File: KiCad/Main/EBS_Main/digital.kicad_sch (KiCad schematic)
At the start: 5 parts

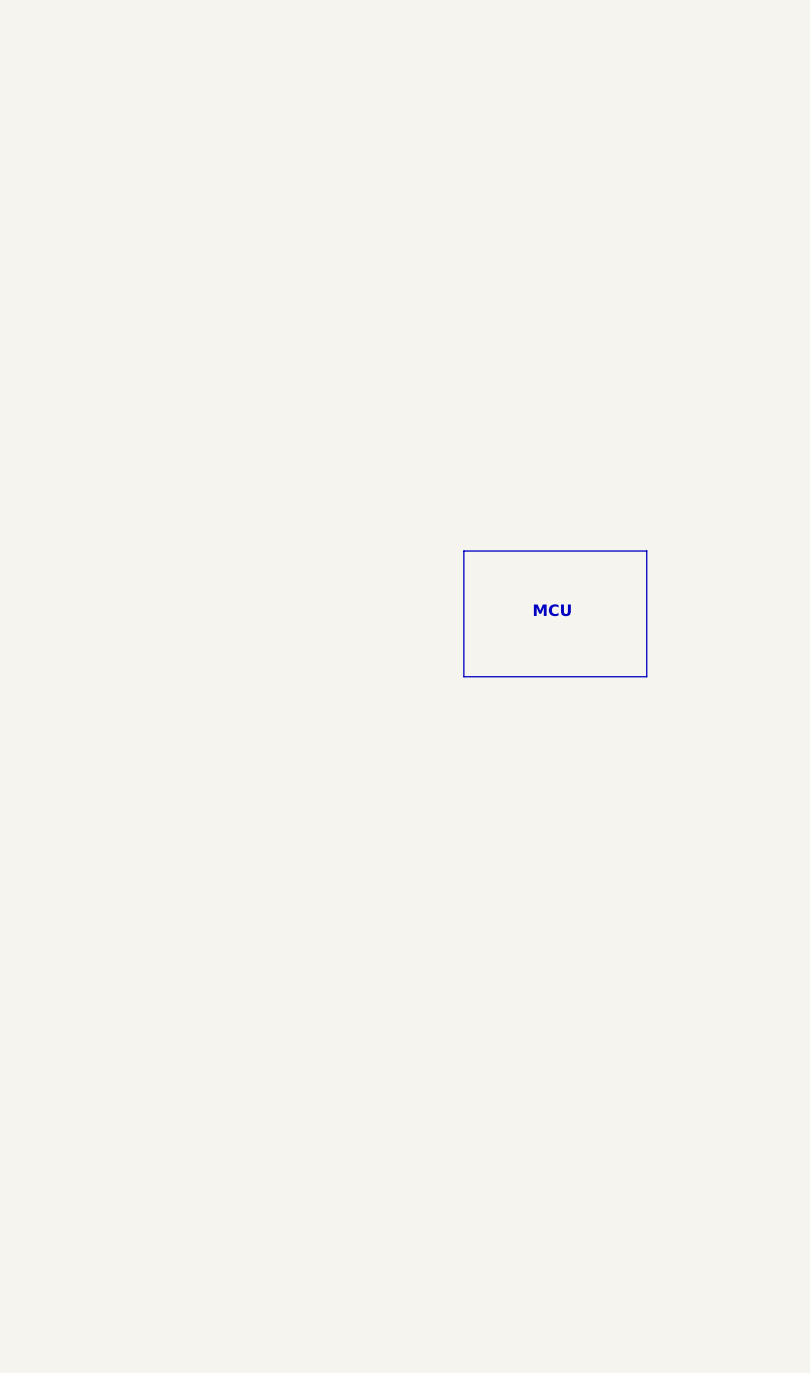
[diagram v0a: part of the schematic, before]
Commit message: found the fpga footprint and added it on schematic
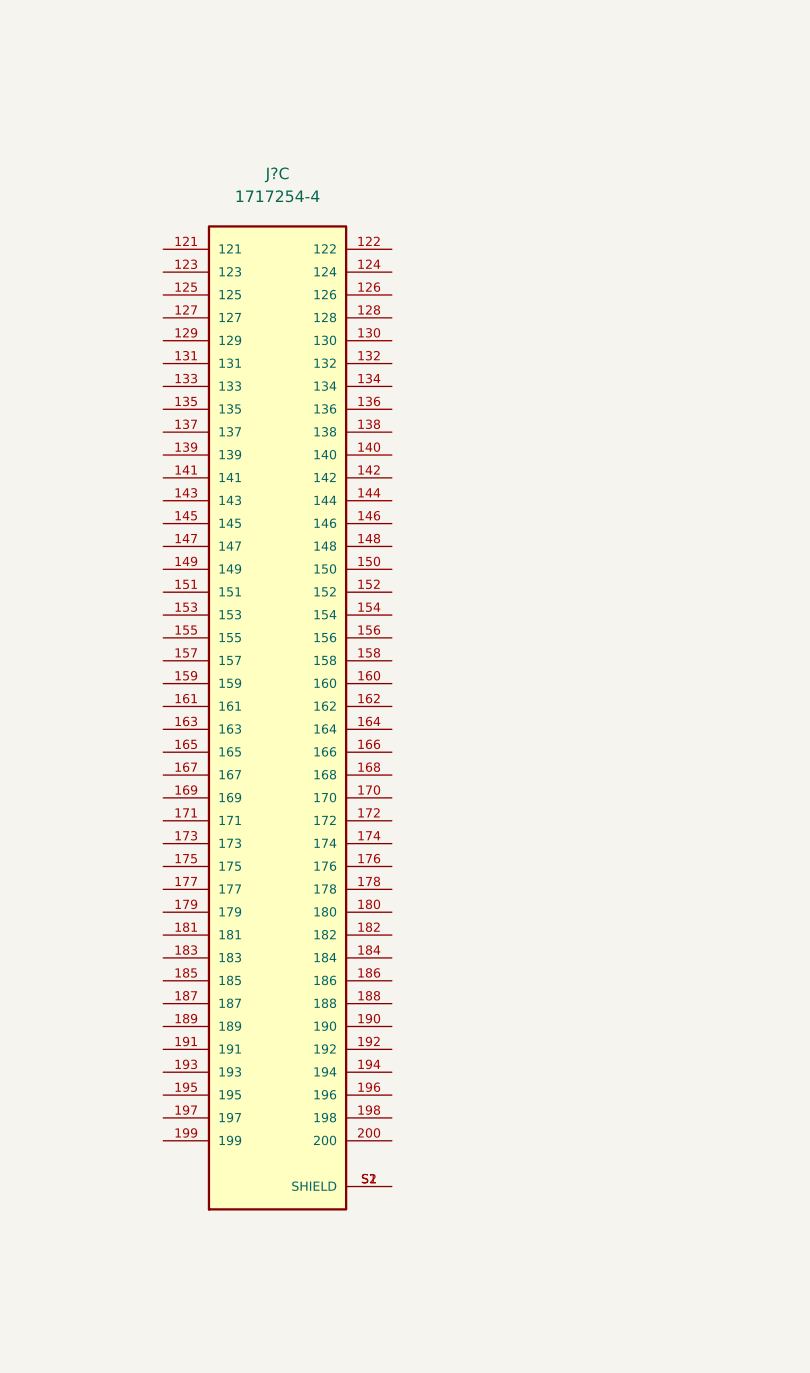
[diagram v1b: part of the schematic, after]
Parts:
- added J?: 1717254-4, TE_1717254-4, symbol 1717254-4:1717254-4
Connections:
- new net: J?.S1 (SHIELD), J?.S2 (SHIELD)
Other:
- note removed: "MCU"

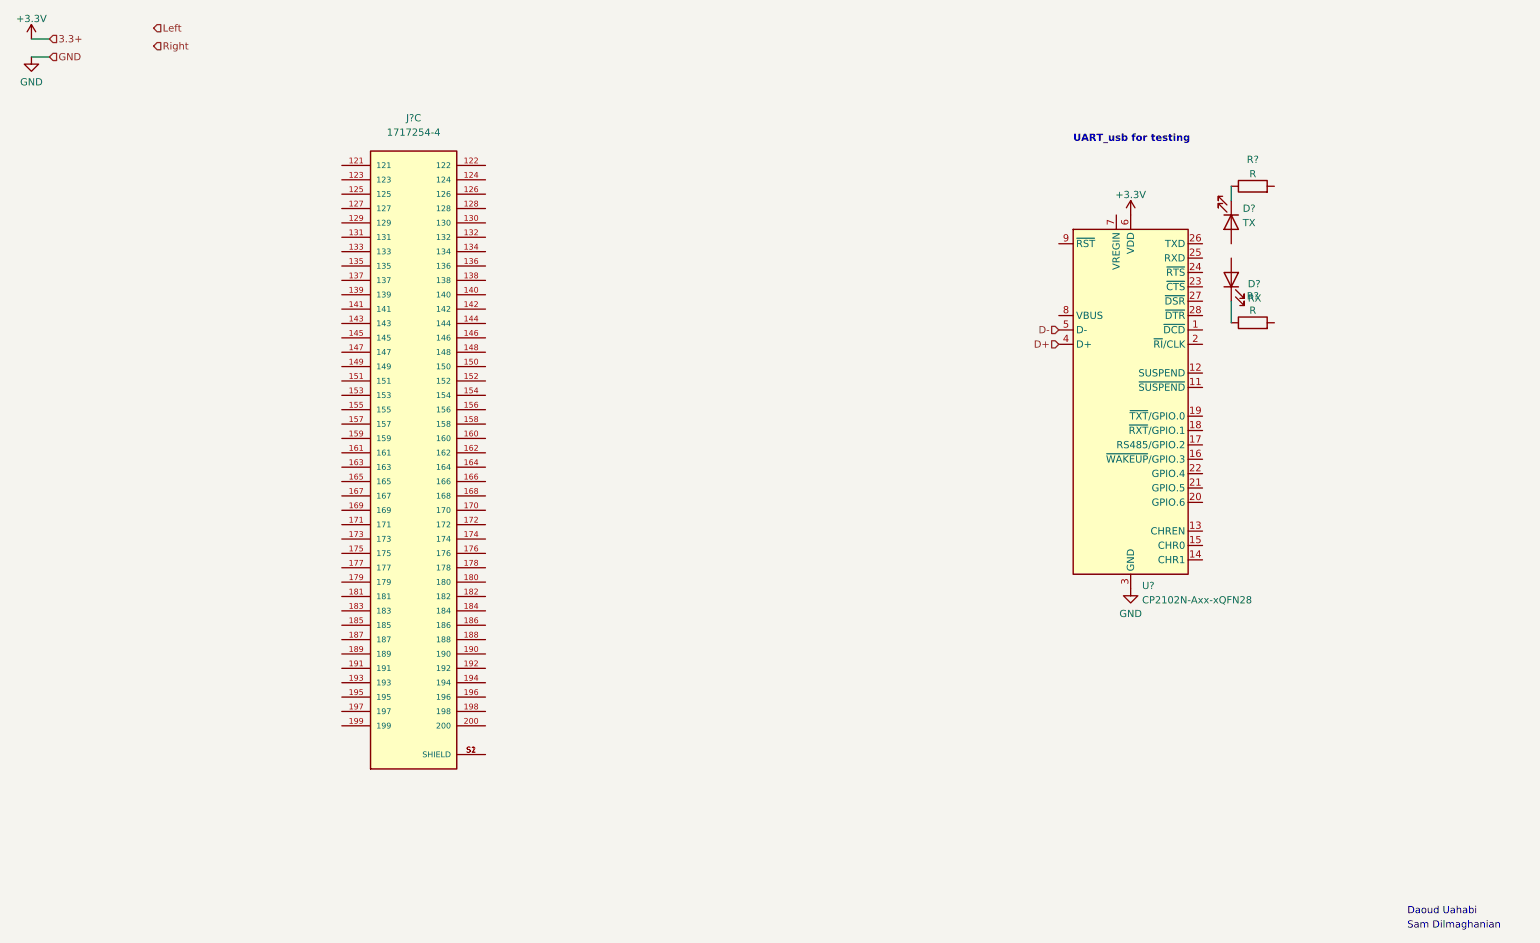
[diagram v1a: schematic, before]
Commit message: added gnd, I2C, USB signals
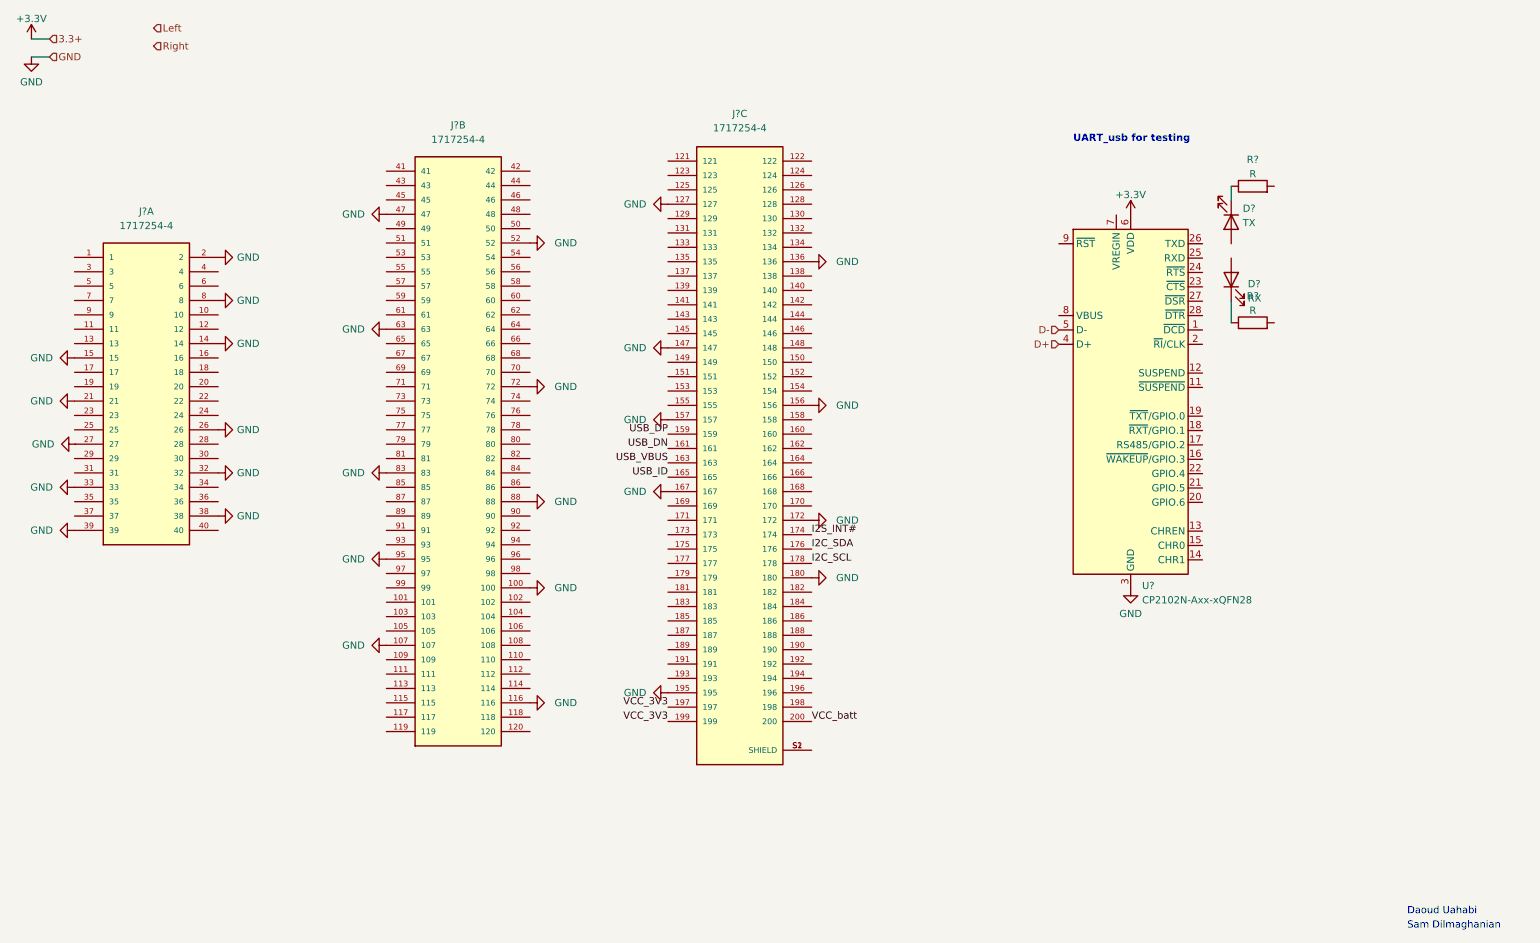
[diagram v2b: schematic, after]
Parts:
- added J? (x2): 1717254-4, TE_1717254-4, symbol 1717254-4:1717254-4
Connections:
- net GND: now also J?.127, J?.136, J?.147, J?.156, J?.157, J?.167, J?.172, J?.180, J?.195, J?.100, J?.107, J?.116, J?.14, J?.15, J?.2, J?.21, J?.26, J?.32, J?.33, J?.38, J?.39, J?.47, J?.52, J?.63, J?.72, J?.8, J?.83, J?.88, J?.95
- net USB_DP: now reaches J?.159
- net USB_DN: now reaches J?.161
- net USB_VBUS: now reaches J?.163
- net USB_ID: now reaches J?.165
- net I2S_INT#: now reaches J?.174
- net I2C_SDA: now reaches J?.176
- net I2C_SCL: now reaches J?.178
- net VCC_3V3: now reaches J?.197
- net VCC_3V3: now also J?.199
- net VCC_batt: now reaches J?.200
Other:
- moved on the sheet: J?C

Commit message: UART
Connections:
- net GND: now also J?.27
- net UART_RX: now reaches J?.153
- net UART_TX: now reaches J?.155
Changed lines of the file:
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@@
+    (stroke (width 0) (type default) (color 0 0 0 0))
+  )
+  (wire (pts (xy 135.382 96.012) (xy 135.382 95.25))
+    (stroke (width 0) (type default) (color 0 0 0 0))
+  )
+  (wire (pts (xy 135.382 101.092) (xy 135.382 100.33))
     (stroke (width 0) (type default) (color 0 0 0 0))
   )
@@
   )
   (wire (pts (xy 22.86 22.86) (xy 26.035 22.86))
+    (stroke (width 0) (type default) (color 0 0 0 0))
+  )
+  (wire (pts (xy 160.782 116.586) (xy 160.782 115.57))
+    (stroke (width 0) (type default) (color 0 0 0 0))
+  )
+  (wire (pts (xy 135.382 144.526) (xy 135.382 143.51))
+    (stroke (width 0) (type default) (color 0 0 0 0))
+  )
+  (wire (pts (xy 135.382 93.472) (xy 135.382 92.71))
+    (stroke (width 0) (type default) (color 0 0 0 0))
+  )
+  (wire (pts (xy 135.382 141.986) (xy 135.382 140.97))
+    (stroke (width 0) (type default) (color 0 0 0 0))
+  )
+  (wire (pts (xy 160.782 114.046) (xy 160.782 113.03))
+    (stroke (width 0) (type default) (color 0 0 0 0))
+  )
+  (wire (pts (xy 160.782 111.506) (xy 160.782 110.49))
+    (stroke (width 0) (type default) (color 0 0 0 0))
+  )
+  (wire (pts (xy 135.382 98.552) (xy 135.382 97.79))
     (stroke (width 0) (type default) (color 0 0 0 0))
   )
@@
     (effects (font (size 1.27 1.27)) (justify left bottom))
   )
-  (label "USB_DP" (at 135.382 92.71 180)
-    (effects (font (size 1.27 1.27)) (justify right bottom))
-  )
-  (label "VCC_3V3" (at 135.382 143.51 180)
-    (effects (font (size 1.27 1.27)) (justify right bottom))
-  )
-  (label "I2C_SCL" (at 160.782 115.57 0)
+  (label "USB_DP" (at 135.382 93.472 180)
+    (effects (font (size 1.27 1.27)) (justify right bottom))
+  )
+  (label "UART_RX" (at 135.382 85.09 180)
+    (effects (font (size 1.27 1.27)) (justify right bottom))
+  )
+  (label "VCC_3V3" (at 135.382 144.526 180)
+    (effects (font (size 1.27 1.27)) (justify right bottom))
+  )
+  (label "I2C_SCL" (at 160.782 116.586 0)
     (effects (font (size 1.27 1.27)) (justify left bottom))
   )
@@
     (effects (font (size 1.27 1.27)) (justify left bottom))
   )
-  (label "USB_ID" (at 135.382 100.33 180)
-    (effects (font (size 1.27 1.27)) (justify right bottom))
-  )
-  (label "VCC_3V3" (at 135.382 140.97 180)
-    (effects (font (size 1.27 1.27)) (justify right bottom))
-  )
-  (label "I2S_INT#" (at 160.782 110.49 0)
-    (effects (font (size 1.27 1.27)) (justify left bottom))
-  )
-  (label "I2C_SDA" (at 160.782 113.03 0)
-    (effects (font (size 1.27 1.27)) (justify left bottom))
-  )
-  (label "USB_DN" (at 135.382 95.25 180)
-    (effects (font (size 1.27 1.27)) (justify right bottom))
-  )
-  (label "USB_VBUS" (at 135.382 97.79 180)
+  (label "USB_ID" (at 135.382 101.092 180)
+    (effects (font (size 1.27 1.27)) (justify right bottom))
+  )
+  (label "VCC_3V3" (at 135.382 141.986 180)
+    (effects (font (size 1.27 1.27)) (justify right bottom))
+  )
+  (label "I2S_INT#" (at 160.782 111.506 0)
+    (effects (font (size 1.27 1.27)) (justify left bottom))
+  )
+  (label "I2C_SDA" (at 160.782 114.046 0)
+    (effects (font (size 1.27 1.27)) (justify left bottom))
+  )
+  (label "USB_DN" (at 135.382 96.012 180)
+    (effects (font (size 1.27 1.27)) (justify right bottom))
+  )
+  (label "UART_TX" (at 135.382 87.63 180)
+    (effects (font (size 1.27 1.27)) (justify right bottom))
+  )
+  (label "USB_VBUS" (at 135.382 98.552 180)
     (effects (font (size 1.27 1.27)) (justify right bottom))
   )
@@
     (pin "2")
   )
-  (symbol (lib_id "power:GND") (at 30.734 94.488 270) (unit 1)
-    (in_bom yes) (on_board yes) (fields_autoplaced)
-    (property "Reference" "#PWR?" (id 0) (at 24.384 94.488 0)
-      (effects (font (size 1.27 1.27)) hide)
-    )
-    (property "Value" "GND" (id 1) (at 26.924 94.4879 90)
-      (effects (font (size 1.27 1.27)) (justify right))
-    )
-    (property "Footprint" "" (id 2) (at 30.734 94.488 0)
-      (effects (font (size 1.27 1.27)) hide)
-    )
-    (property "Datasheet" "" (id 3) (at 30.734 94.488 0)
-      (effects (font (size 1.27 1.27)) hide)
-    )
+  (symbol (lib_id "power:GND") (at 30.48 94.488 270) (unit 1)
+    (in_bom yes) (on_board yes) (fields_autoplaced)
+    (property "Reference" "#PWR?" (id 0) (at 24.13 94.488 0)
+      (effects (font (size 1.27 1.27)) hide)
+    )
+    (property "Value" "GND" (id 1) (at 26.67 94.4879 90)
+      (effects (font (size 1.27 1.27)) (justify right))
+    )
+    (property "Footprint" "" (id 2) (at 30.48 94.488 0)
+      (effects (font (size 1.27 1.27)) hide)
+    )
+    (property "Datasheet" "" (id 3) (at 30.48 94.488 0)
+      (effects (font (size 1.27 1.27)) hide)
+    )
